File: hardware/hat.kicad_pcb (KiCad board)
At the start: 4 copper layers, 65 x 56 mm, 142 parts, among them J101 Raspberry_Pi_2_3, J102 Boot, J201 USB Power In, K201 CONN_3, P101 Debug, P201 Black, P301 CON-SENSOR2, P302 CON-SENSOR2, P303 CON-SENSOR2, P304 CON-SENSOR2, P305 CON-SENSOR2, P306 CON-SENSOR2, P307 CON-SENSOR2, P308 CON-SENSOR2, Q101 2N7002P, Q102 2N7002P, Q103 NTR2101P, Q104 NTR2101P, U101 XMC1404, U102 LD1117, U201 MAX17260_LS, U202 BQ2407X, U203 AOZ1212, U204 MIC2253, U205 AP7333-33SAG-7, U301 74AHC244, U302 74AHC244, U303 74AHC244, U304 74AHC244, X101 16MHz, X102 32.768kHz

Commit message: specify parts
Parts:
- D201: value D -> RB058LAM150TR
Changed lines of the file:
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@@
-(kicad_pcb (version 4) (host pcbnew 4.0.2+dfsg1-stable)
+(kicad_pcb (version 4) (host pcbnew 4.0.7-e2-6376~61~ubuntu18.04.1)
   (general
     (links 478)
     (no_connects 0)
-    (area 166.150469 25.950469 231.249531 82.049531)
+    (area 165.999999 25.799999 231.400001 83.625001)
     (thickness 1.6)
     (drawings 50)
@@
     (aux_axis_origin 166.2 26)
     (grid_origin 166.2 26)
-    (visible_elements FFFF5F7F)
+    (visible_elements FFFF9F7F)
     (pcbplotparams
       (layerselection 0x00020_00000000)
@@
       (effects (font (size 0.2 0.2) (thickness 0.05)) (justify mirror))
     )
-    (fp_text value D (at 0.52 0.49 90) (layer B.Fab)
-      (effects (font (size 0.2 0.2) (thickness 0.05)) (justify mirror))
-    )
+    (fp_text value RB058LAM150TR (at 0.52 0.49 90) (layer B.Fab)
+      (effects (font (size 0.2 0.2) (thickness 0.05)) (justify mirror))
+    )

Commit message: values specified
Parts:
- C218: value TBD -> 100nF
- R206: value TBD -> 10m
- R213: value TBD -> 59k
- R216: value TBD -> 33k
- R218: value Varistor -> VC120626D580DP
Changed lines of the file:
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@@
   (page A4)
   (layers
-    (0 F.Cu signal)
+    (0 F.Cu signal hide)
     (1 GND signal hide)
     (2 VCC signal hide)
@@
     (aux_axis_origin 166.2 26)
     (grid_origin 166.2 26)
-    (visible_elements FFFF9F7F)
+    (visible_elements FFFFDF7F)
     (pcbplotparams
       (layerselection 0x00020_00000000)
@@
       (effects (font (size 0.2 0.2) (thickness 0.05)))
     )
-    (fp_text value TBD (at 0.05 -0.375) (layer F.Fab)
+    (fp_text value 100nF (at 0.05 -0.375) (layer F.Fab)
       (effects (font (size 0.2 0.2) (thickness 0.05)))
     )
@@
       (effects (font (size 0.29972 0.29972) (thickness 0.07493)))
     )
-    (fp_text value TBD (at 0 0.6) (layer F.Fab)
+    (fp_text value 10m (at 0 0.6) (layer F.Fab)
       (effects (font (size 0.29972 0.29972) (thickness 0.07493)))
     )
@@
       (effects (font (size 0.2 0.2) (thickness 0.05)) (justify mirror))
     )
-    (fp_text value TBD (at 0.05 0.375) (layer B.Fab)
+    (fp_text value 59k (at 0.05 0.375) (layer B.Fab)
       (effects (font (size 0.2 0.2) (thickness 0.05)) (justify mirror))
     )
@@
       (effects (font (size 0.2 0.2) (thickness 0.05)))
     )
-    (fp_text value TBD (at 0.05 -0.375 270) (layer F.Fab)
+    (fp_text value 33k (at 0.05 -0.375 270) (layer F.Fab)
       (effects (font (size 0.2 0.2) (thickness 0.05)))
     )
@@
       (effects (font (size 0.3 0.3) (thickness 0.075)))
     )
-    (fp_text value Varistor (at 0 -0.65) (layer F.Fab)
+    (fp_text value VC120626D580DP (at 0 -0.65) (layer F.Fab)
       (effects (font (size 0.3 0.3) (thickness 0.075)))
     )

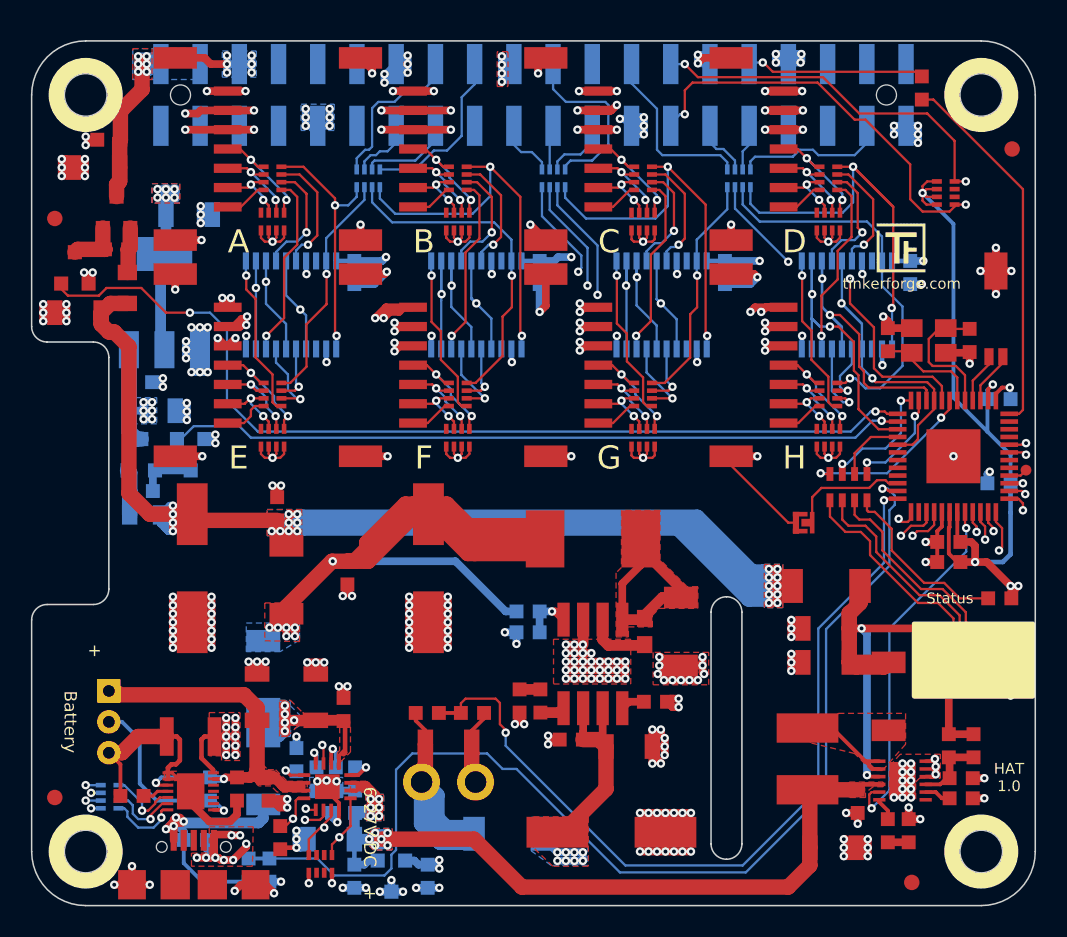
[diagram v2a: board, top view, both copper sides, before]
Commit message: fix raspberry pi hat female header footprint
not every signal fixed
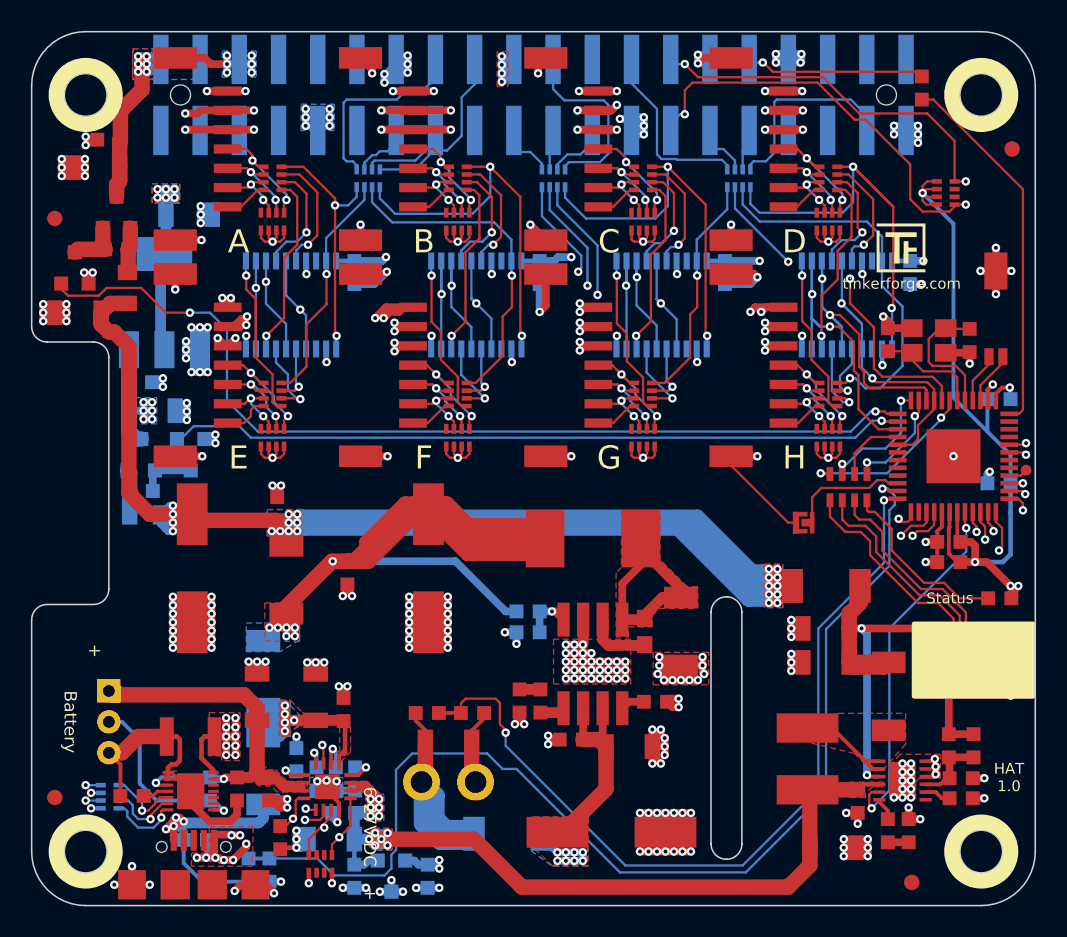
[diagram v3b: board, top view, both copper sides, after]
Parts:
- C218: value 100nF -> TBD
- D201: value RB058LAM150TR -> D
- R206: value 10m -> TBD
- R213: value 59k -> TBD
- R216: value 33k -> TBD
- R218: value VC120626D580DP -> Varistor
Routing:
- net Net-(J101-Pad37): track 10.0 -> 13.0 mm
- net Net-(J101-Pad16): track 10.3 -> 12.4 mm
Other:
- board size 65 x 56 mm -> 65 x 56.6 mm
- board text added: "Stecker falsch herum?"

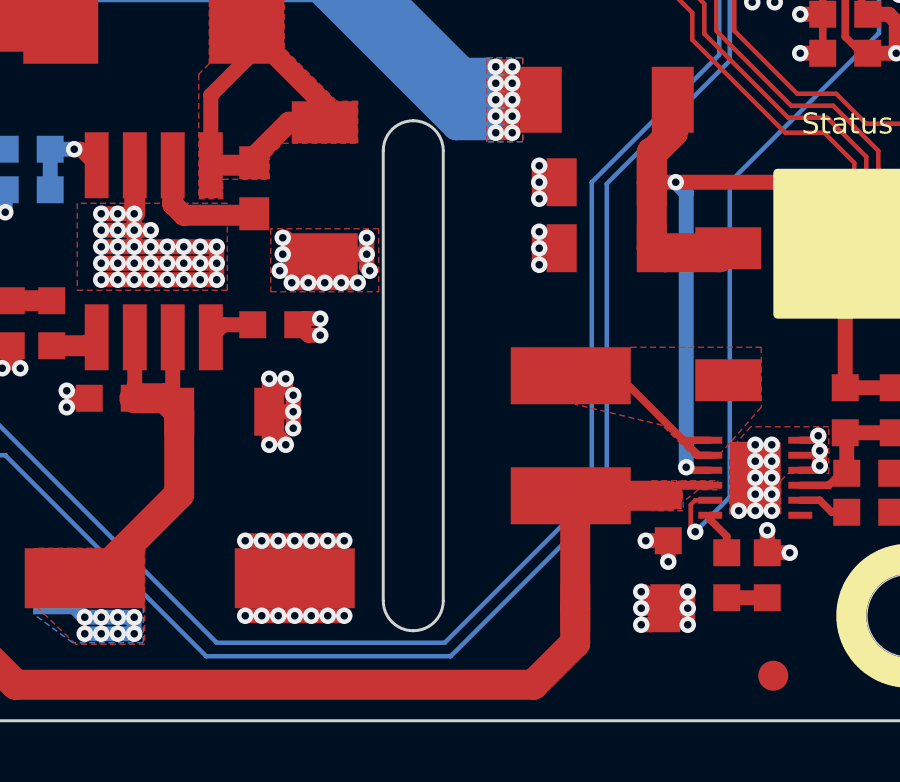
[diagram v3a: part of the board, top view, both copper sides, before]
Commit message: raspberry pi footprint increase, not every signal fixed
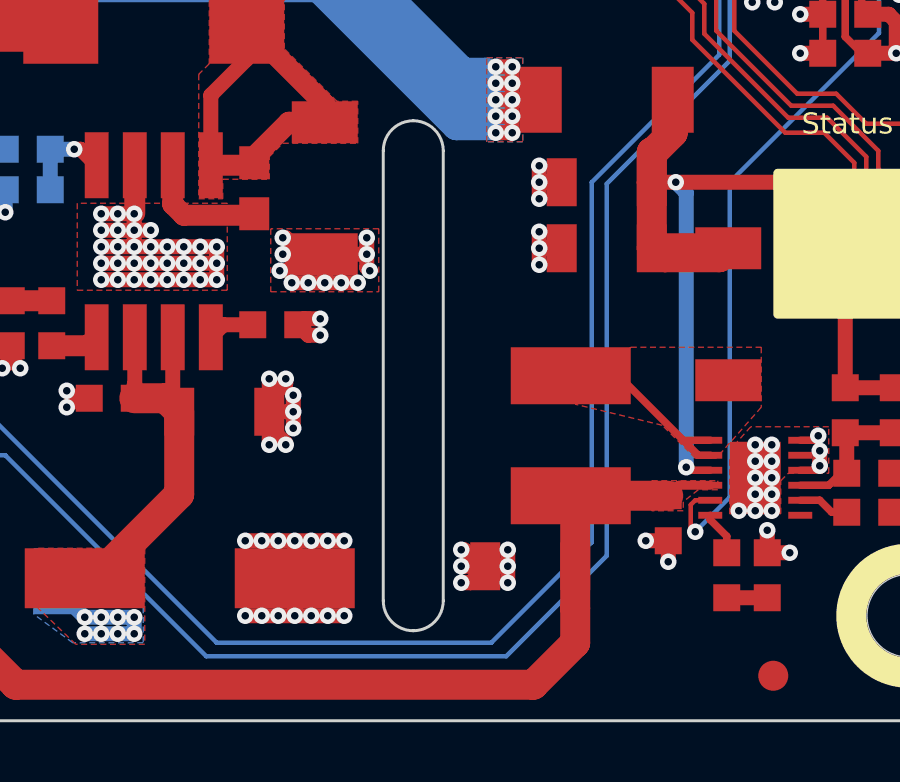
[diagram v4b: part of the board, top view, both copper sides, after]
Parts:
- C218: value TBD -> 100nF
- D101: value blue -> green
- D102: value green -> blue
- moved C227 3.31 mm to (215.1, 76.8), turned to 180 degrees
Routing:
- net USB-IN-VOLTAGE: track 73.1 -> 74.2 mm
- net DC-IN-VOLTAGE: track 54.7 -> 55.6 mm
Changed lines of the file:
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@@
     (aux_axis_origin 166.2 26)
     (grid_origin 166.2 26)
-    (visible_elements FFFFDF7F)
+    (visible_elements FFFEDF7F)
     (pcbplotparams
       (layerselection 0x00020_00000000)
@@
       (effects (font (size 0.2 0.2) (thickness 0.05)))
     )
-    (fp_text value TBD (at 0.05 -0.375) (layer F.Fab)
+    (fp_text value 100nF (at 0.05 -0.375) (layer F.Fab)
       (effects (font (size 0.2 0.2) (thickness 0.05)))
     )
@@
       (effects (font (size 0.2 0.2) (thickness 0.05)))
     )
-    (fp_text value blue (at 0.75 0.45 180) (layer F.Fab)
+    (fp_text value green (at 0.75 0.45 180) (layer F.Fab)
       (effects (font (size 0.2 0.2) (thickness 0.05)))
     )
@@
   )
   (module kicad-libraries:C1206 (layer F.Cu)
-    (at 218.1 78.25)
+    (at 215.1 76.85 180)
     (attr smd)
-    (fp_text reference C227 (at 0 0.5375) (layer F.Fab)
+    (fp_text reference C227 (at 0 0.5375 180) (layer F.Fab)
       (effects (font (size 0.3 0.3) (thickness 0.075)))
     )
-    (fp_text value 10uF/16V (at 0 -0.65) (layer F.Fab)
+    (fp_text value 10uF/16V (at 0 -0.65 180) (layer F.Fab)
       (effects (font (size 0.3 0.3) (thickness 0.075)))
     )
@@
     (fp_line (start 2.25044 1.09982) (end 2.25044 -1.09982) (layer F.Fab) (width 0.001))
     (fp_line (start 2.25044 -1.09982) (end -2.25044 -1.09982) (layer F.Fab) (width 0.001))
-    (pad 1 smd rect (at -1.50114 0) (size 1.00076 1.6002) (layers F.Cu F.Paste F.Mask)
+    (pad 1 smd rect (at -1.50114 0 180) (size 1.00076 1.6002) (layers F.Cu F.Paste F.Mask)
       (net 127 BOOST-IN))
-    (pad 2 smd rect (at 1.50114 0) (size 1.00076 1.6002) (layers F.Cu F.Paste F.Mask)
+    (pad 2 smd rect (at 1.50114 0 180) (size 1.00076 1.6002) (layers F.Cu F.Paste F.Mask)
       (net 2 GND))
     (model Capacitors_SMD/C_1206.wrl
@@
       (effects (font (size 0.2 0.2) (thickness 0.05)))
     )
-    (fp_text value green (at 0.75 0.45 180) (layer F.Fab)
+    (fp_text value blue (at 0.75 0.45 180) (layer F.Fab)
       (effects (font (size 0.2 0.2) (thickness 0.05)))
     )
@@
   (via (at 168.15 33.65) (size 0.55) (drill 0.25) (layers F.Cu B.Cu) (net 2))
   (segment (start 168.15 33.65) (end 168.4 33.65) (width 0.5) (layer F.Cu) (net 2))
-  (segment (start 220.35 78.25) (end 220.35 78.8) (width 0.5) (layer F.Cu) (net 2))
-  (via (at 220.35 78.25) (size 0.55) (drill 0.25) (layers F.Cu B.Cu) (net 2))
-  (via (at 220.35 78.8) (size 0.55) (drill 0.25) (layers F.Cu B.Cu) (net 2))
-  (segment (start 220.35 77.7) (end 220.35 78.25) (width 0.5) (layer F.Cu) (net 2))
-  (segment (start 220.35 78.25) (end 219.60114 78.25) (width 0.5) (layer F.Cu) (net 2))
-  (via (at 220.35 77.7) (size 0.55) (drill 0.25) (layers F.Cu B.Cu) (net 2))
+  (segment (start 214.35 76.85) (end 214.35 77.4) (width 0.5) (layer F.Cu) (net 2))
+  (via (at 214.35 76.85) (size 0.55) (drill 0.25) (layers F.Cu B.Cu) (net 2))
+  (via (at 214.35 77.4) (size 0.55) (drill 0.25) (layers F.Cu B.Cu) (net 2))
+  (segment (start 214.35 76.3) (end 214.35 76.85) (width 0.5) (layer F.Cu) (net 2))
+  (segment (start 214.35 76.85) (end 213.60114 76.85) (width 0.5) (layer F.Cu) (net 2))
+  (via (at 214.35 76.3) (size 0.55) (drill 0.25) (layers F.Cu B.Cu) (net 2))
   (segment (start 224.75 73) (end 224.75 73.5) (width 0.5) (layer F.Cu) (net 2))
   (segment (start 224.6 73.65) (end 224.75 73.5) (width 0.25) (layer F.Cu) (net 2))
@@
   (segment (start 223 76.4) (end 223 75.65) (width 0.5) (layer F.Cu) (net 2))
   (via (at 223 75.65) (size 0.55) (drill 0.25) (layers F.Cu B.Cu) (net 2))
-  (segment (start 219.60114 78.25) (end 219.60114 78.29886) (width 0.5) (layer F.Cu) (net 2))
-  (segment (start 219.60114 78.29886) (end 219.1 78.8) (width 0.5) (layer F.Cu) (net 2))
-  (via (at 218.8 78.8) (size 0.55) (drill 0.25) (layers F.Cu B.Cu) (net 2))
-  (segment (start 219.1 78.8) (end 218.8 78.8) (width 0.5) (layer F.Cu) (net 2))
-  (segment (start 219.60114 78.25) (end 219.45 78.25) (width 0.5) (layer F.Cu) (net 2))
-  (segment (start 219.45 78.25) (end 218.9 77.7) (width 0.5) (layer F.Cu) (net 2))
-  (via (at 218.8 77.7) (size 0.55) (drill 0.25) (layers F.Cu B.Cu) (net 2))
-  (segment (start 218.9 77.7) (end 218.8 77.7) (width 0.5) (layer F.Cu) (net 2))
-  (segment (start 219.60114 78.25) (end 218.8 78.25) (width 0.5) (layer F.Cu) (net 2))
-  (via (at 218.8 78.25) (size 0.55) (drill 0.25) (layers F.Cu B.Cu) (net 2))
+  (segment (start 213.60114 76.85) (end 213.60114 76.89886) (width 0.5) (layer F.Cu) (net 2))
+  (segment (start 213.60114 76.89886) (end 213.1 77.4) (width 0.5) (layer F.Cu) (net 2))
+  (via (at 212.8 77.4) (size 0.55) (drill 0.25) (layers F.Cu B.Cu) (net 2))
+  (segment (start 213.1 77.4) (end 212.8 77.4) (width 0.5) (layer F.Cu) (net 2))
+  (segment (start 213.60114 76.85) (end 213.45 76.85) (width 0.5) (layer F.Cu) (net 2))
+  (segment (start 213.45 76.85) (end 212.9 76.3) (width 0.5) (layer F.Cu) (net 2))
+  (via (at 212.8 76.3) (size 0.55) (drill 0.25) (layers F.Cu B.Cu) (net 2))
+  (segment (start 212.9 76.3) (end 212.8 76.3) (width 0.5) (layer F.Cu) (net 2))
+  (segment (start 213.60114 76.85) (end 212.8 76.85) (width 0.5) (layer F.Cu) (net 2))
+  (via (at 212.8 76.85) (size 0.55) (drill 0.25) (layers F.Cu B.Cu) (net 2))
   (segment (start 219.7 76) (end 219.7 76.7) (width 0.5) (layer F.Cu) (net 2))
   (via (at 219.7 76.7) (size 0.55) (drill 0.25) (layers F.Cu B.Cu) (net 2))
@@
   (segment (start 221.75 60) (end 221.75 56.4) (width 0.15) (layer B.Cu) (net 59))
   (segment (start 217.65 64.1) (end 221.75 60) (width 0.15) (layer B.Cu) (net 59))
-  (segment (start 217.65 74.65) (end 217.65 64.1) (width 0.15) (layer B.Cu) (net 59))
-  (segment (start 212.45 79.85) (end 217.65 74.65) (width 0.15) (layer B.Cu) (net 59))
-  (segment (start 204.3 79.85) (end 212.45 79.85) (width 0.15) (layer B.Cu) (net 59))
+  (segment (start 217.65 76.5) (end 217.65 64.1) (width 0.15) (layer B.Cu) (net 59))
+  (segment (start 214.3 79.85) (end 217.65 76.5) (width 0.15) (layer B.Cu) (net 59))
+  (segment (start 204.3 79.85) (end 214.3 79.85) (width 0.15) (layer B.Cu) (net 59))
   (segment (start 197.6 73.15) (end 204.3 79.85) (width 0.15) (layer B.Cu) (net 59))
   (segment (start 196.7 73.15) (end 197.6 73.15) (width 0.15) (layer B.Cu) (net 59))
@@
   (segment (start 221.4 55.75) (end 221.4 59.8) (width 0.15) (layer B.Cu) (net 60))
   (segment (start 221.4 59.8) (end 217.15 64.05) (width 0.15) (layer B.Cu) (net 60))
-  (segment (start 217.15 64.05) (end 217.15 74.5) (width 0.15) (layer B.Cu) (net 60))
-  (segment (start 217.15 74.5) (end 212.25 79.4) (width 0.15) (layer B.Cu) (net 60))
-  (segment (start 212.25 79.4) (end 204.65 79.4) (width 0.15) (layer B.Cu) (net 60))
+  (segment (start 217.15 64.05) (end 217.15 76.05) (width 0.15) (layer B.Cu) (net 60))
+  (segment (start 217.15 76.05) (end 213.8 79.4) (width 0.15) (layer B.Cu) (net 60))
+  (segment (start 213.8 79.4) (end 204.65 79.4) (width 0.15) (layer B.Cu) (net 60))
   (segment (start 204.65 79.4) (end 196.9 71.65) (width 0.15) (layer B.Cu) (net 60))
   (segment (start 196.9 71.65) (end 196.9 70.8) (width 0.15) (layer B.Cu) (net 60))

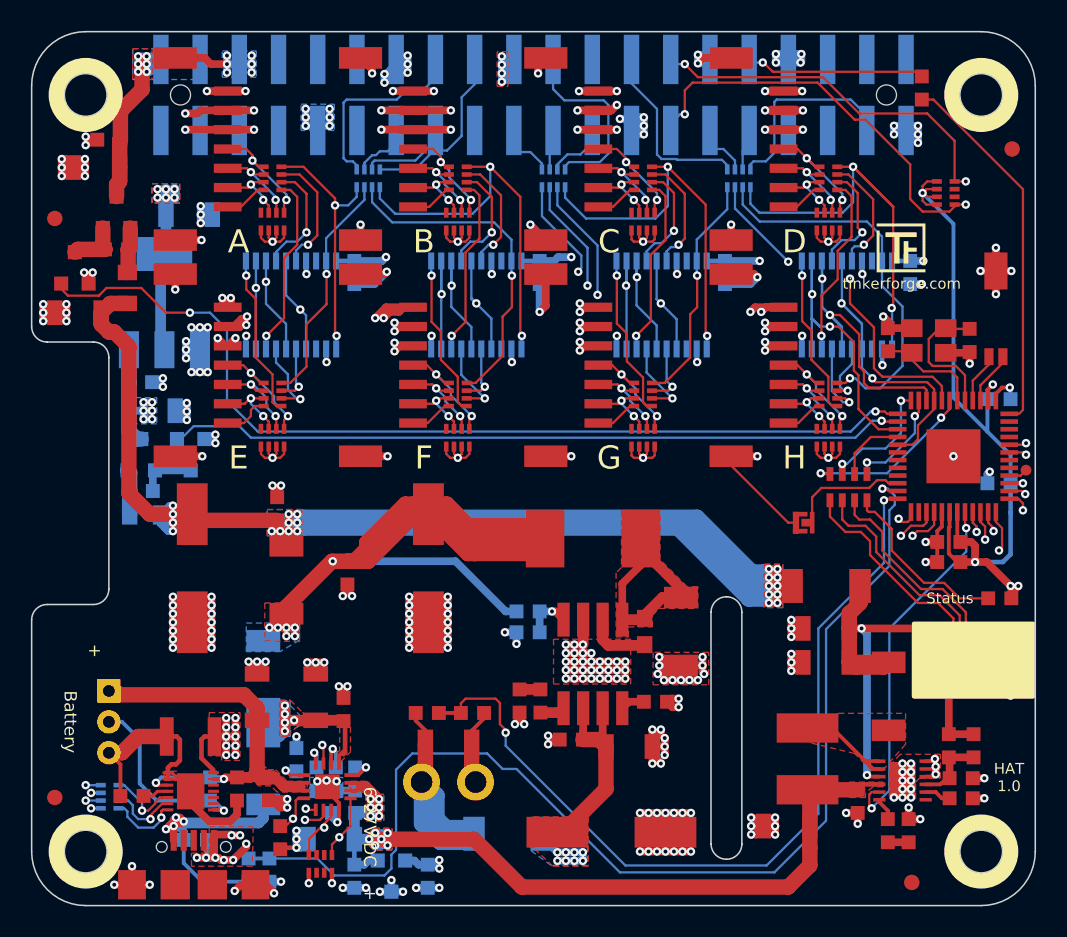
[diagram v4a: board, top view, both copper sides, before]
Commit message: swap cs2 and cs3, fix routing
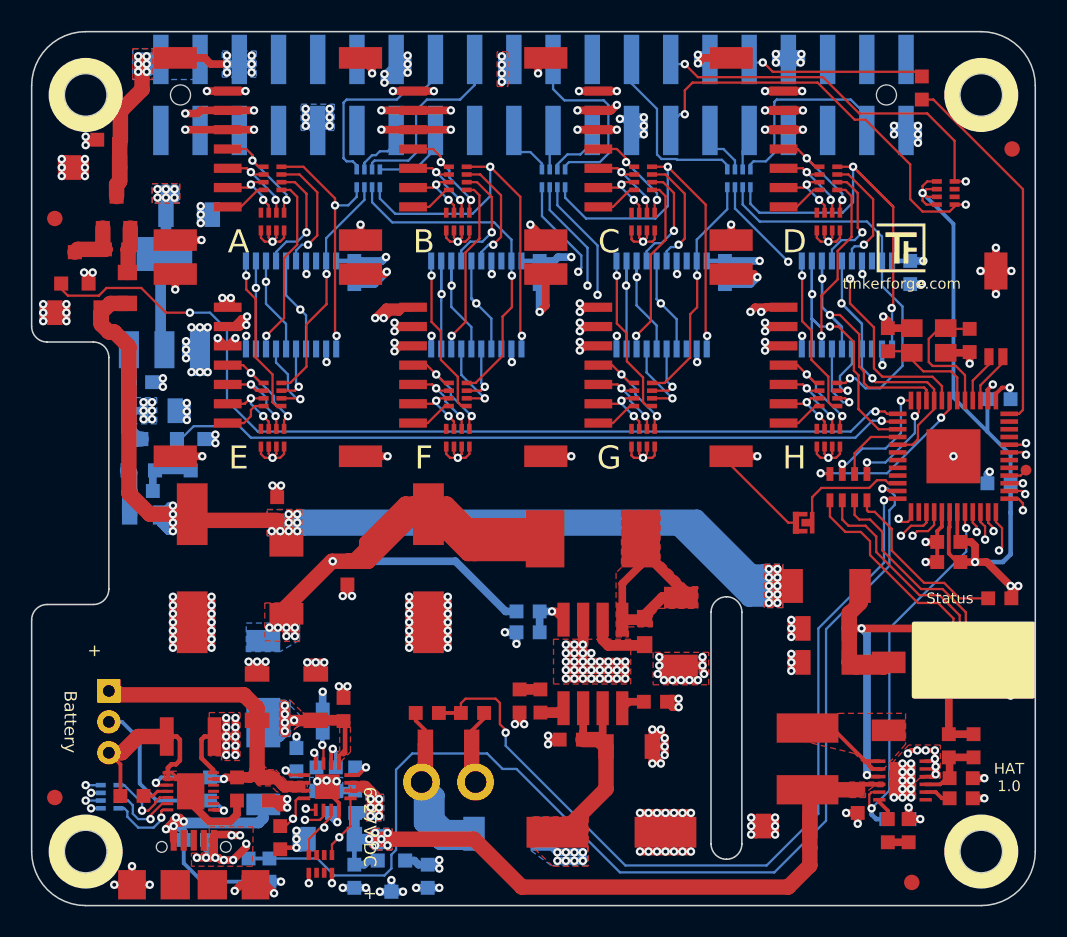
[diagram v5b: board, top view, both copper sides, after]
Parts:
- added R219: 10k, kicad-libraries:R0603F, B.Cu at (185.1, 70.0)
- added R220: 10k, kicad-libraries:R0603F, B.Cu at (222.3, 76.4)
- D201: value D -> RB058LAM150TR
- R206: value TBD -> 10m
- R213: value TBD -> 59k
- R216: value TBD -> 33k
- R218: value Varistor -> VC120626D580DP
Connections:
- RP102 pad 7: Net-(J101-Pad15) -> Net-(J101-Pad18)
- RP102 pad 8: Net-(J101-Pad18) -> Net-(J101-Pad15)
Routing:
- net GND: track 364.5 -> 368.8 mm, vias 317 -> 322
- net BOOST-EN: track 23.4 -> 24.9 mm
- net Net-(J101-Pad18): track 12.4 -> 13.6 mm
- net CHG-SYSOFF: track 57.6 -> 58.4 mm
